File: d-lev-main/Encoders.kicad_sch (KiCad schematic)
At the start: 8 parts, among them SW1 RotaryEncoder_Switch, SW2 RotaryEncoder_Switch, SW3 RotaryEncoder_Switch, SW4 RotaryEncoder_Switch, SW5 RotaryEncoder_Switch, SW6 RotaryEncoder_Switch, SW7 RotaryEncoder_Switch, SW8 RotaryEncoder_Switch

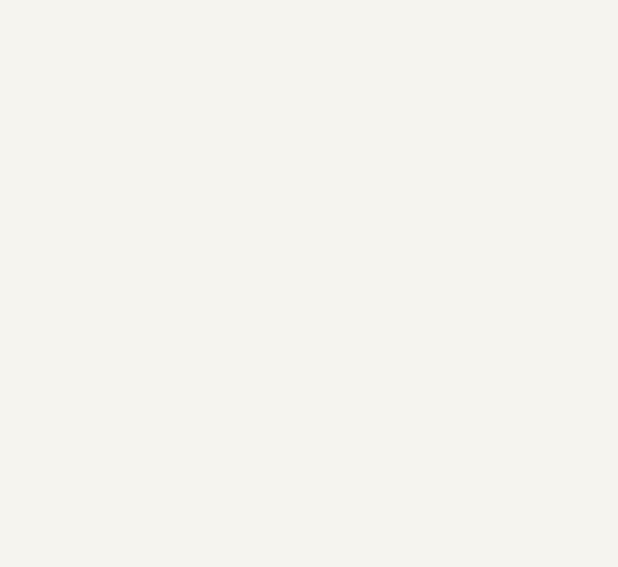
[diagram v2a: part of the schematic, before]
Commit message: clean up 3d models
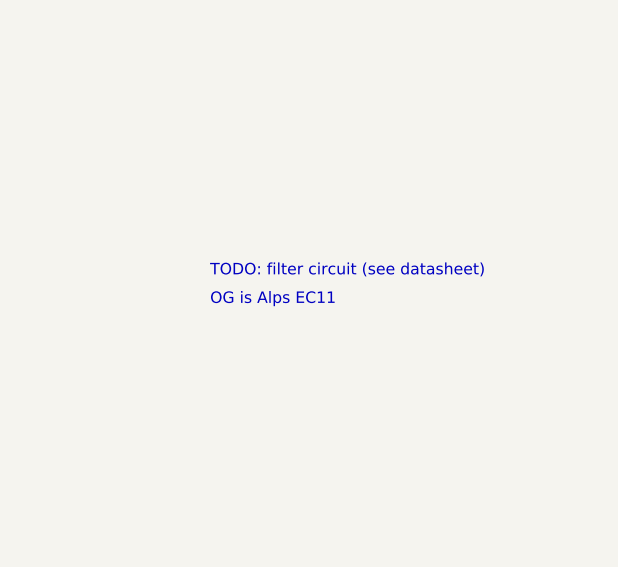
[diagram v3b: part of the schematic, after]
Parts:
- SW1, SW2, SW3, SW4, SW5, SW6, SW7, SW8: footprint (none) -> d-lev:PEC11S9215FS0015
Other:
- note added: "OG is Alps EC11"
- note added: "TODO: filter circuit (see datasheet)"
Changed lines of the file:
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@@
     (stroke (width 0) (type default))
+  )
+  (text "OG is Alps EC11" (at 173.99 66.04 0)
+    (effects (font (size 1.27 1.27)) (justify left bottom))
+  )
+  (text "TODO: filter circuit (see datasheet)" (at 173.99 62.865 0)
+    (effects (font (size 1.27 1.27)) (justify left bottom))
   )
   (label "S0" (at 48.26 22.86 0) (fields_autoplaced)
@@
       (effects (font (size 1.27 1.27)))
     )
-    (property "Footprint" "" (at 76.2 61.976 0)
-      (effects (font (size 1.27 1.27)) hide)
-    )
-    (property "Datasheet" "~" (at 72.39 59.436 0)
+    (property "Footprint" "d-lev:PEC11S9215FS0015" (at 76.2 61.976 0)
+      (effects (font (size 1.27 1.27)) hide)
+    )
+    (property "Datasheet" "https://www.mouser.com/datasheet/2/54/pec11s-953234.pdf" (at 72.39 59.436 0)
       (effects (font (size 1.27 1.27)) hide)
     )
@@
       (effects (font (size 1.27 1.27)))
     )
-    (property "Footprint" "" (at 76.2 106.426 0)
-      (effects (font (size 1.27 1.27)) hide)
-    )
-    (property "Datasheet" "~" (at 72.39 103.886 0)
+    (property "Footprint" "d-lev:PEC11S9215FS0015" (at 76.2 106.426 0)
+      (effects (font (size 1.27 1.27)) hide)
+    )
+    (property "Datasheet" "https://www.mouser.com/datasheet/2/54/pec11s-953234.pdf" (at 72.39 103.886 0)
       (effects (font (size 1.27 1.27)) hide)
     )
@@
       (effects (font (size 1.27 1.27)))
     )
-    (property "Footprint" "" (at 76.2 41.656 0)
-      (effects (font (size 1.27 1.27)) hide)
-    )
-    (property "Datasheet" "~" (at 72.39 39.116 0)
+    (property "Footprint" "d-lev:PEC11S9215FS0015" (at 76.2 41.656 0)
+      (effects (font (size 1.27 1.27)) hide)
+    )
+    (property "Datasheet" "https://www.mouser.com/datasheet/2/54/pec11s-953234.pdf" (at 72.39 39.116 0)
       (effects (font (size 1.27 1.27)) hide)
     )
@@
       (effects (font (size 1.27 1.27)))
     )
-    (property "Footprint" "" (at 76.2 21.336 0)
-      (effects (font (size 1.27 1.27)) hide)
-    )
-    (property "Datasheet" "~" (at 72.39 18.796 0)
+    (property "Footprint" "d-lev:PEC11S9215FS0015" (at 76.2 21.336 0)
+      (effects (font (size 1.27 1.27)) hide)
+    )
+    (property "Datasheet" "https://www.mouser.com/datasheet/2/54/pec11s-953234.pdf" (at 72.39 18.796 0)
       (effects (font (size 1.27 1.27)) hide)
     )
@@
       (effects (font (size 1.27 1.27)))
     )
-    (property "Footprint" "" (at 76.2 82.296 0)
-      (effects (font (size 1.27 1.27)) hide)
-    )
-    (property "Datasheet" "~" (at 72.39 79.756 0)
+    (property "Footprint" "d-lev:PEC11S9215FS0015" (at 76.2 82.296 0)
+      (effects (font (size 1.27 1.27)) hide)
+    )
+    (property "Datasheet" "https://www.mouser.com/datasheet/2/54/pec11s-953234.pdf" (at 72.39 79.756 0)
       (effects (font (size 1.27 1.27)) hide)
     )
@@
       (effects (font (size 1.27 1.27)))
     )
-    (property "Footprint" "" (at 76.2 167.386 0)
-      (effects (font (size 1.27 1.27)) hide)
-    )
-    (property "Datasheet" "~" (at 72.39 164.846 0)
+    (property "Footprint" "d-lev:PEC11S9215FS0015" (at 76.2 167.386 0)
+      (effects (font (size 1.27 1.27)) hide)
+    )
+    (property "Datasheet" "https://www.mouser.com/datasheet/2/54/pec11s-953234.pdf" (at 72.39 164.846 0)
       (effects (font (size 1.27 1.27)) hide)
     )
@@
       (effects (font (size 1.27 1.27)))
     )
-    (property "Footprint" "" (at 76.2 126.746 0)
-      (effects (font (size 1.27 1.27)) hide)
-    )
-    (property "Datasheet" "~" (at 72.39 124.206 0)
+    (property "Footprint" "d-lev:PEC11S9215FS0015" (at 76.2 126.746 0)
+      (effects (font (size 1.27 1.27)) hide)
+    )
+    (property "Datasheet" "https://www.mouser.com/datasheet/2/54/pec11s-953234.pdf" (at 72.39 124.206 0)
       (effects (font (size 1.27 1.27)) hide)
     )
@@
       (effects (font (size 1.27 1.27)))
     )
-    (property "Footprint" "" (at 76.2 147.066 0)
-      (effects (font (size 1.27 1.27)) hide)
-    )
-    (property "Datasheet" "~" (at 72.39 144.526 0)
-      (effects (font (size 1.27 1.27)) hide)
-    )
+    (property "Footprint" "d-lev:PEC11S9215FS0015" (at 76.2 147.066 0)
+      (effects (font (size 1.27 1.27)) hide)
+    )
+    (property "Datasheet" "https://www.mouser.com/datasheet/2/54/pec11s-953234.pdf" (at 72.39 144.526 0)
+      (effects (font (size 1.27 1.27)) hide)
+    )

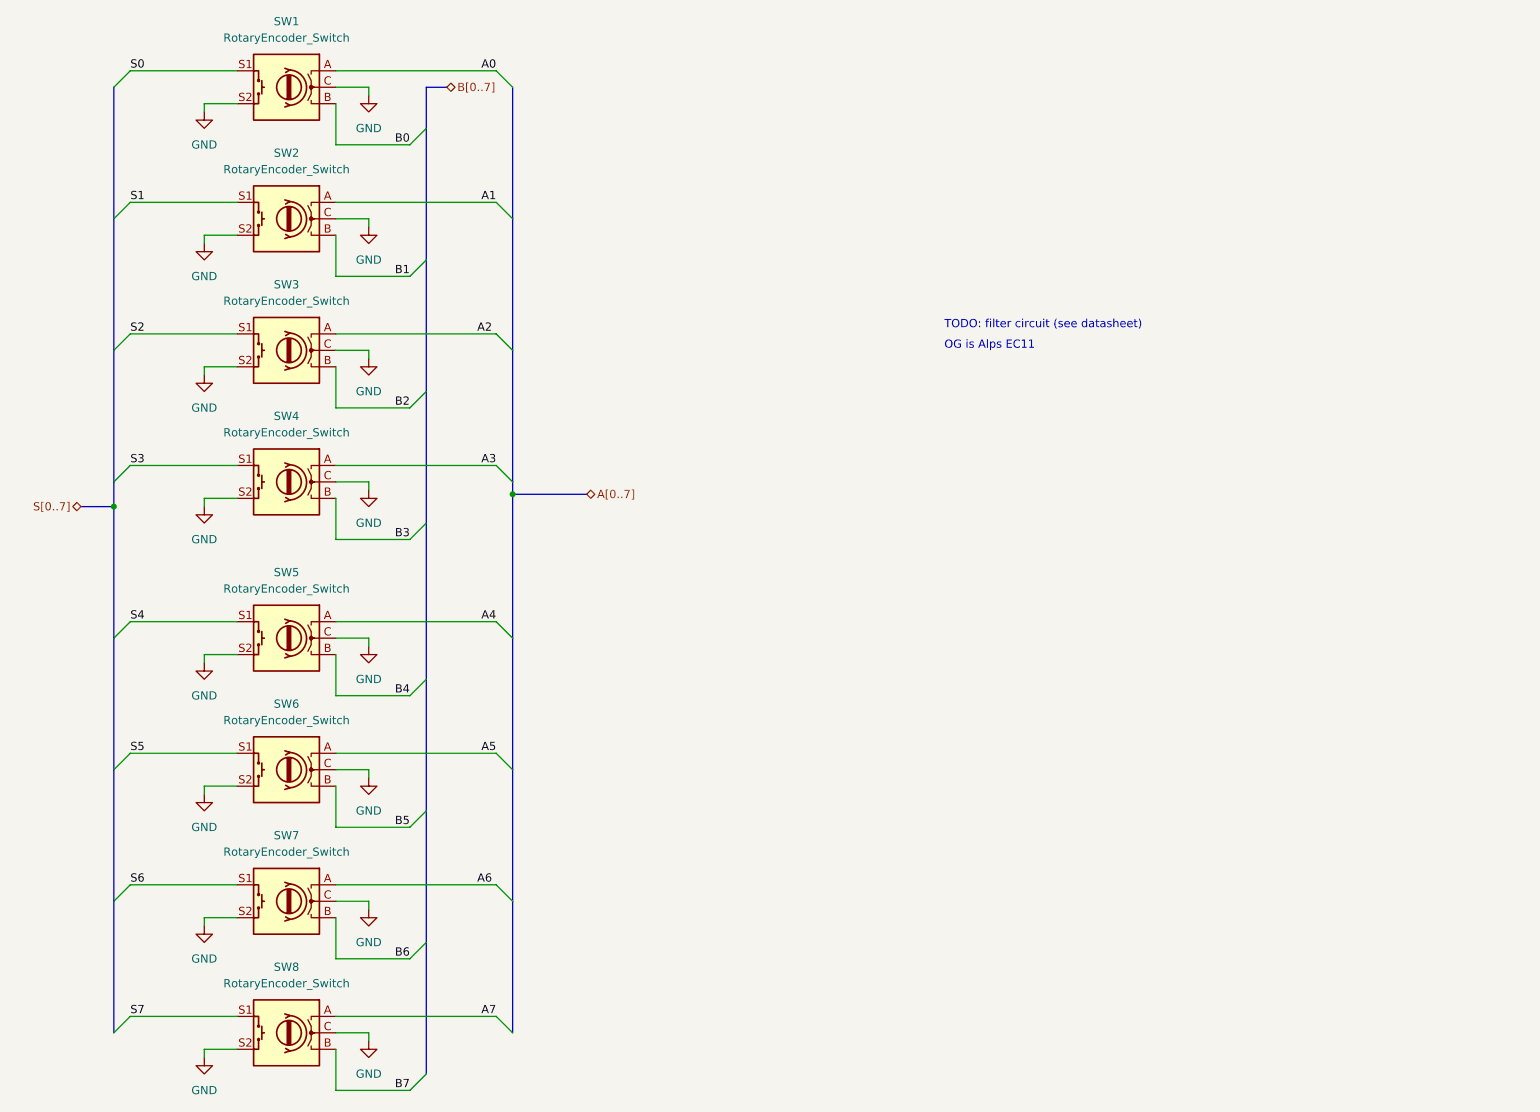
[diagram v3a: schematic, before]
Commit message: Level shifters and rearrange encoders
* WIP: use net buses more effectively to organize encoder signals
* Add application note for level shifters
* Add level shifters for UART, change MIDI level shifter BJT to FET
* Add MIDI_HI pull-up on d-lev-io board
* Add/change some footprints
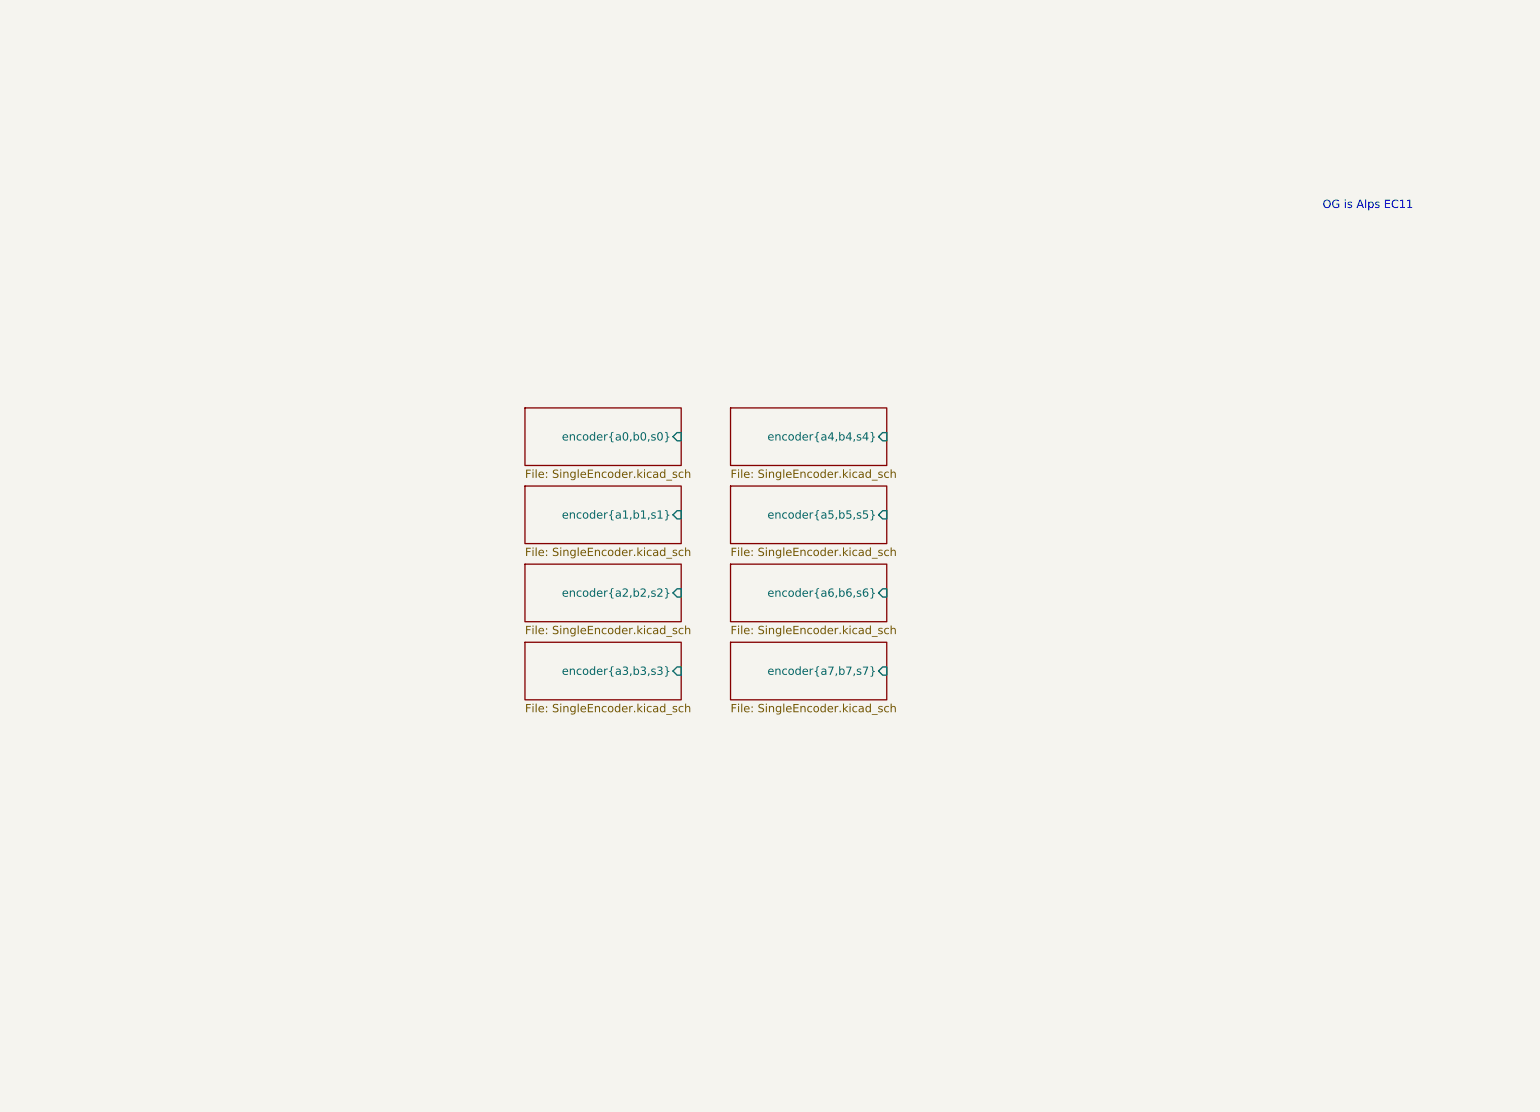
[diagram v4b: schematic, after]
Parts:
- removed SW1, SW2, SW3, SW4, SW5, SW6, SW7, SW8: RotaryEncoder_Switch, d-lev:PEC11S9215FS0015, symbol Device:RotaryEncoder_Switch
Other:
- added sheet SingleEncoder10 (SingleEncoder.kicad_sch)
- added sheet SingleEncoder3 (SingleEncoder.kicad_sch)
- added sheet SingleEncoder4 (SingleEncoder.kicad_sch)
- added sheet SingleEncoder5 (SingleEncoder.kicad_sch)
- added sheet SingleEncoder6 (SingleEncoder.kicad_sch)
- added sheet SingleEncoder7 (SingleEncoder.kicad_sch)
- added sheet SingleEncoder8 (SingleEncoder.kicad_sch)
- added sheet SingleEncoder9 (SingleEncoder.kicad_sch)
- note removed: "TODO: filter circuit (see datasheet)"

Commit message: more encoder bus mangling
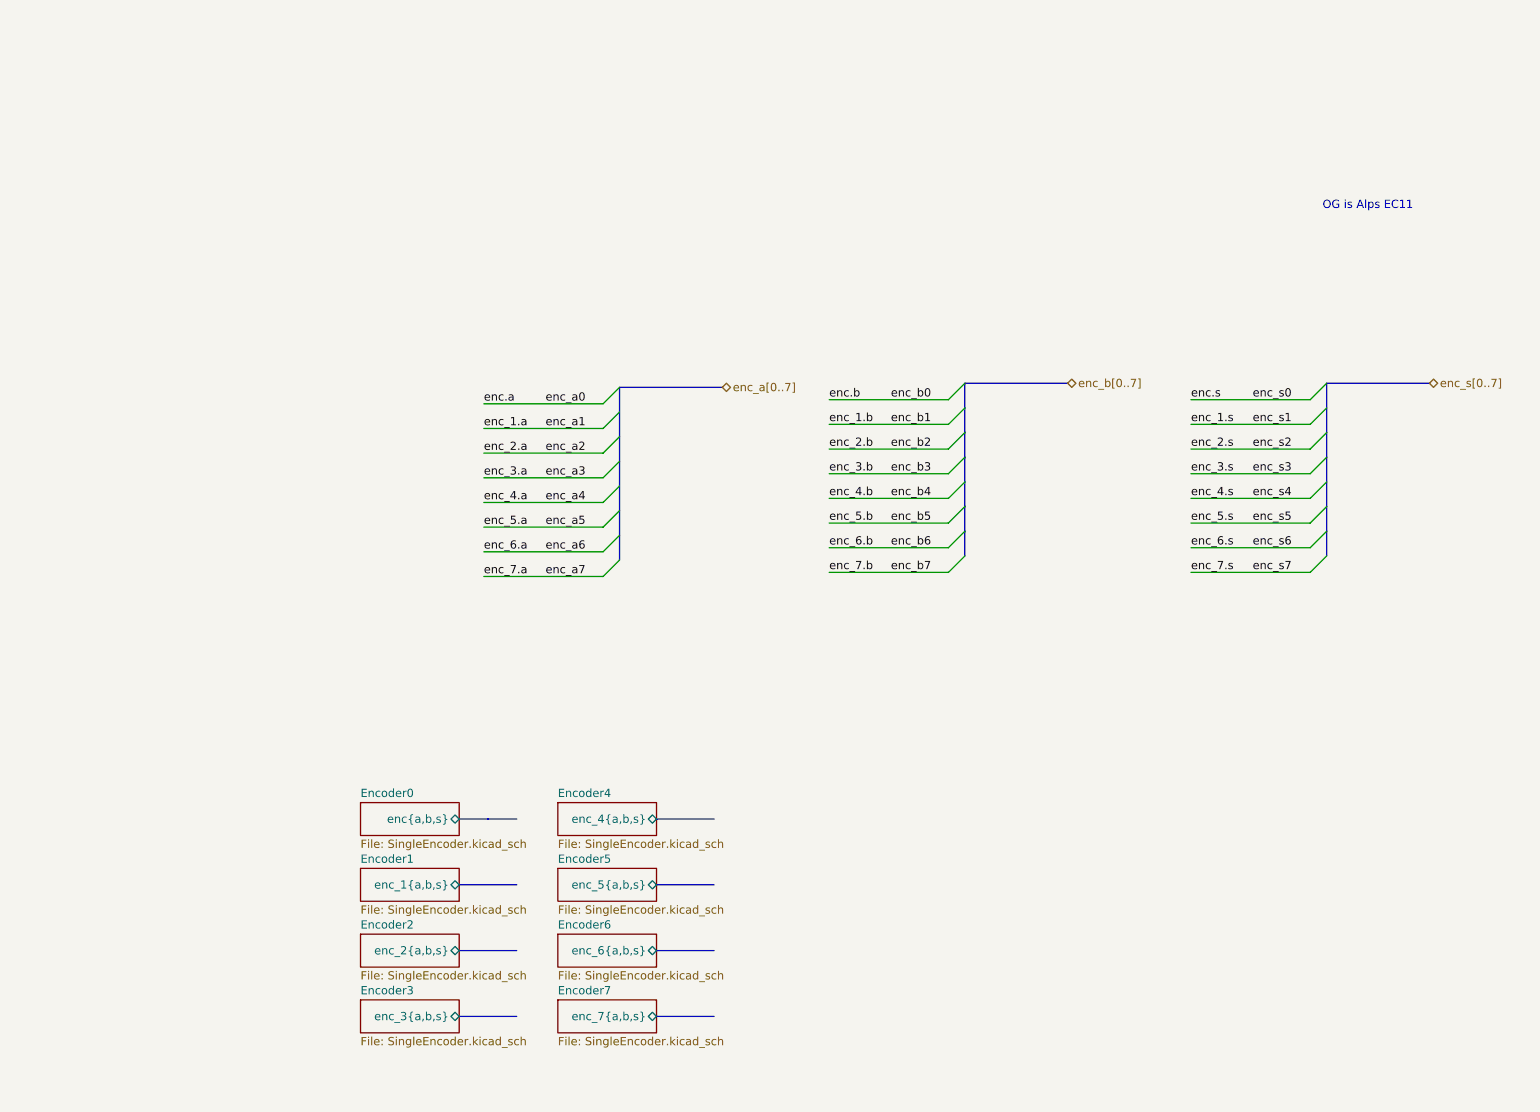
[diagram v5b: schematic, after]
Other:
- removed sheet SingleEncoder10
- removed sheet SingleEncoder3
- removed sheet SingleEncoder4
- removed sheet SingleEncoder5
- removed sheet SingleEncoder6
- removed sheet SingleEncoder7
- removed sheet SingleEncoder8
- removed sheet SingleEncoder9
- added sheet Encoder0 (SingleEncoder.kicad_sch)
- added sheet Encoder1 (SingleEncoder.kicad_sch)
- added sheet Encoder2 (SingleEncoder.kicad_sch)
- added sheet Encoder3 (SingleEncoder.kicad_sch)
- added sheet Encoder4 (SingleEncoder.kicad_sch)
- added sheet Encoder5 (SingleEncoder.kicad_sch)
- added sheet Encoder6 (SingleEncoder.kicad_sch)
- added sheet Encoder7 (SingleEncoder.kicad_sch)

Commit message: Small changes to 3D models and footprints; fixed bus routing of encoder signals
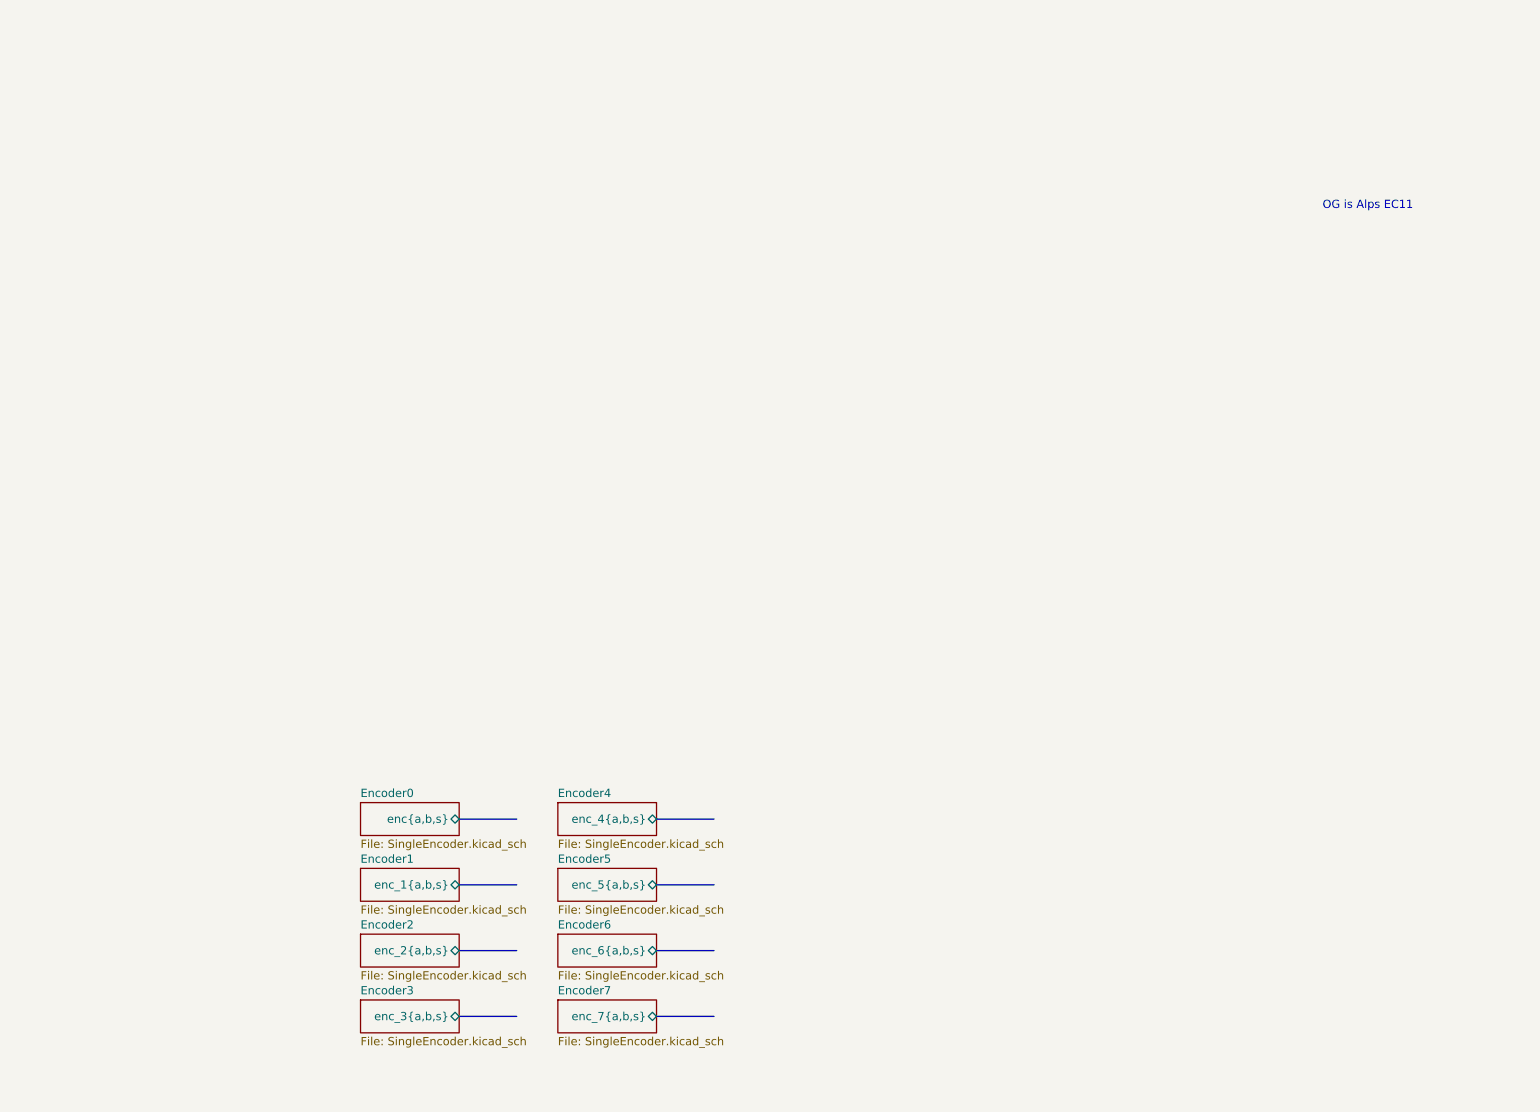
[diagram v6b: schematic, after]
